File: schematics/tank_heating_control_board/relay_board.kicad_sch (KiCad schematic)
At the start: 30 parts, among them J1 Programming Header, J2 Power IN from battery, J3 Power OUT to heater, K1 AZ2150-1AE-24DEF, Q1 MMBF170, SW1 SW_DIP_x04, U1 JST I2C Connector, U2 JST I2C Connector, U3 PIC16F1826-ISO, U4 INA180A1

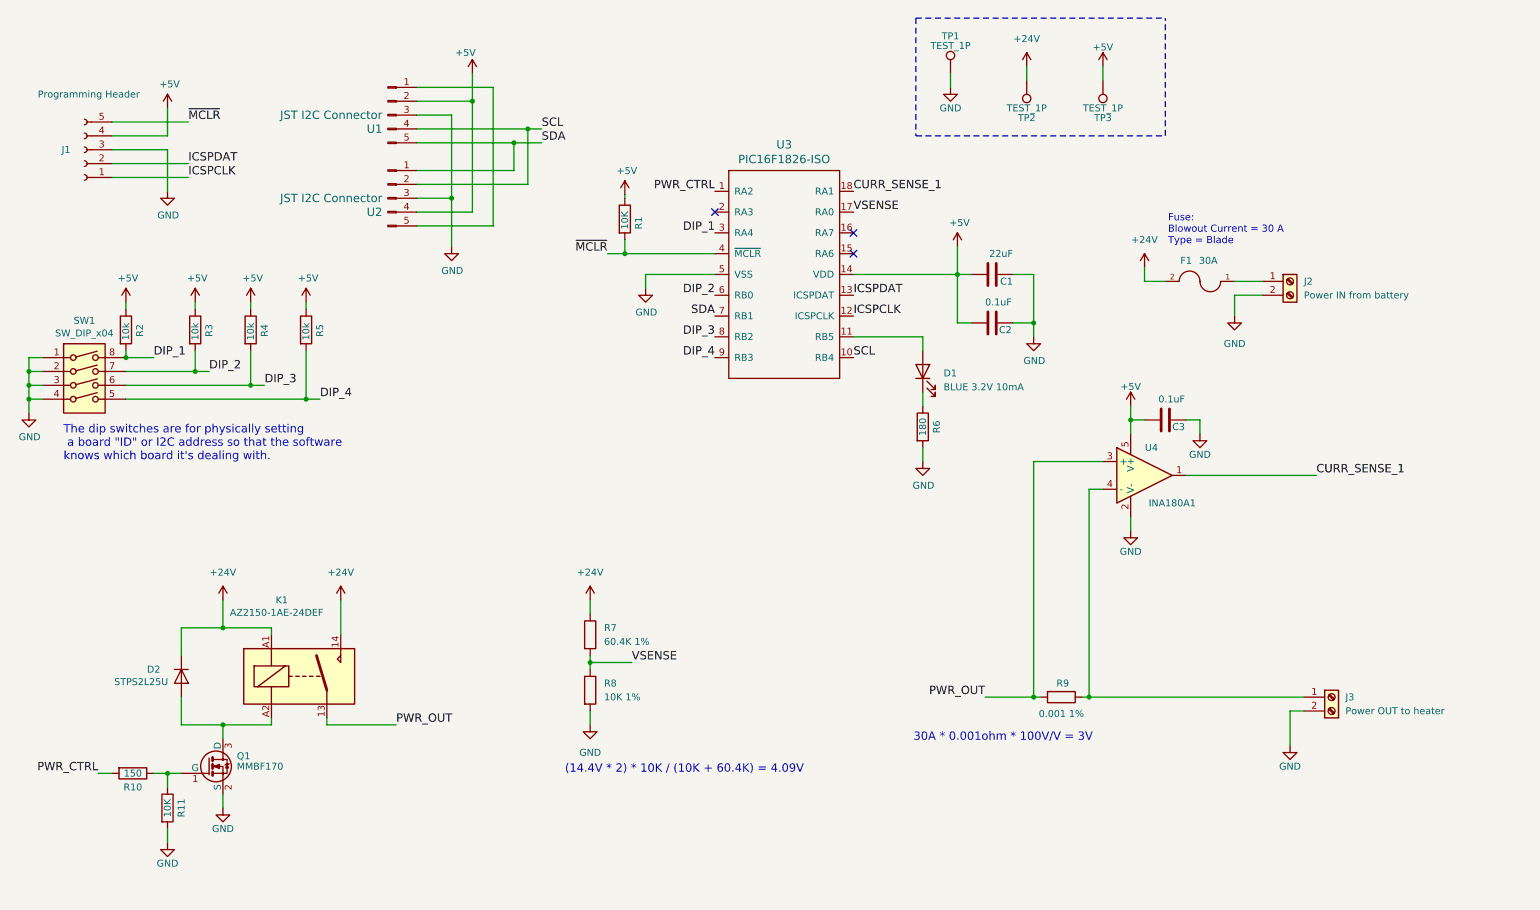
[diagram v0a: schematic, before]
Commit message: Add thermistor and voltage sensing to schematics
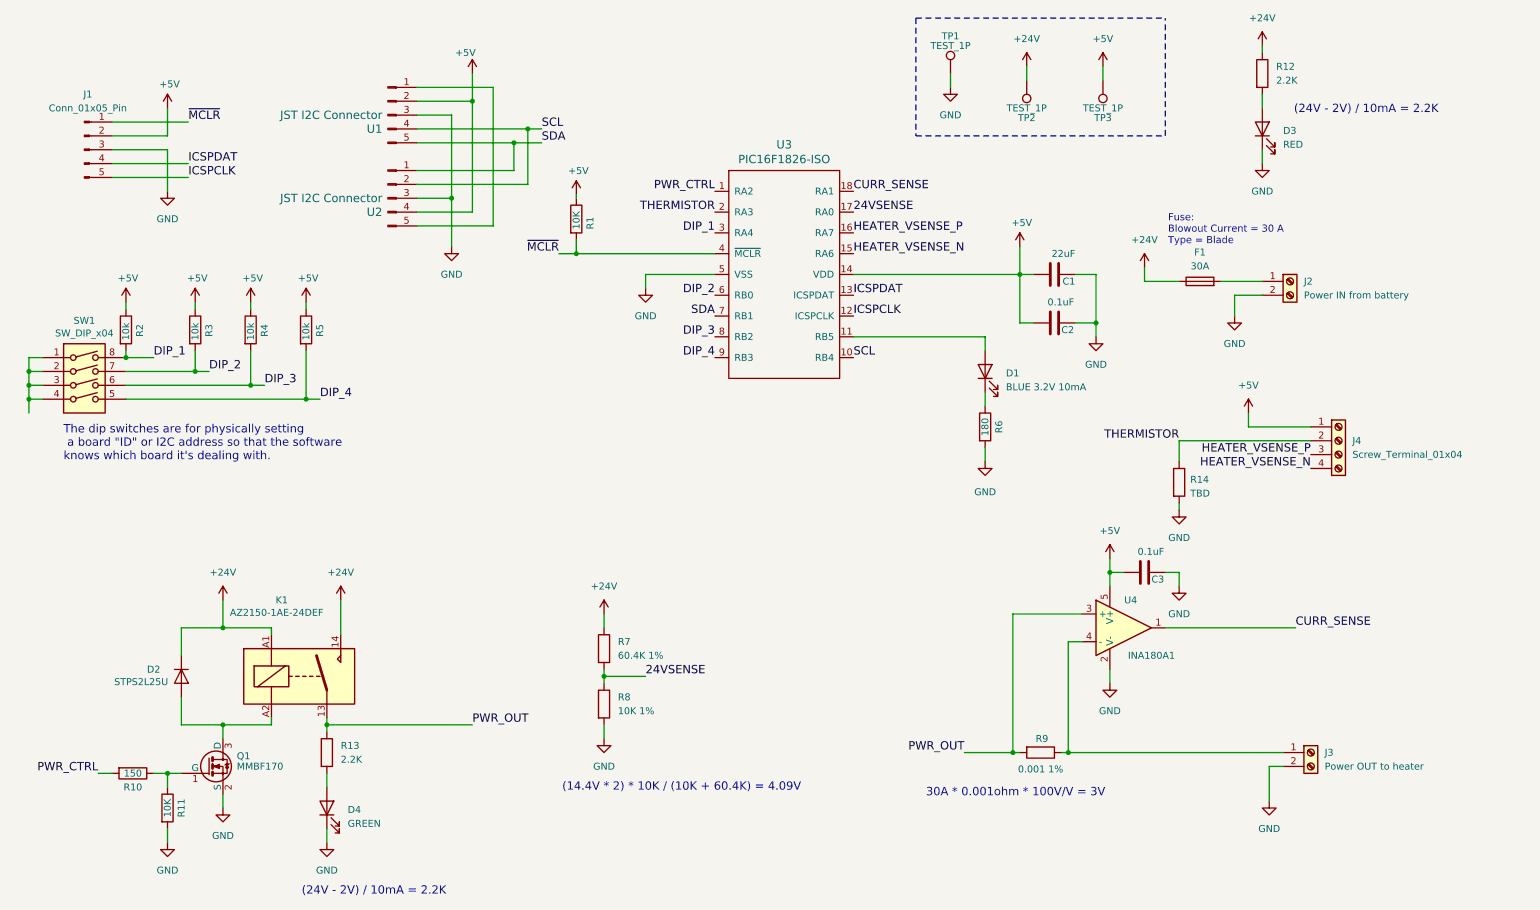
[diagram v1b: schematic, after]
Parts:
- removed F1: 30A, custom:littlefuse_01000020Z, symbol relay_board:FUSE-rlcs_relay_board
- removed J1: Programming Header, custom:PinHeader_5x2.54_SMD_90deg_952-3198-1-ND, symbol Connector:Conn_01x05_Female
- added D3: RED, LED_SMD:LED_1206_3216Metric_Pad1.42x1.75mm_HandSolder, symbol Device:LED
- added D4: GREEN, LED_SMD:LED_1206_3216Metric_Pad1.42x1.75mm_HandSolder, symbol Device:LED
- added F1: 30A, custom:3557-10_KEY, symbol Device:Fuse
- added J1: Conn_01x05_Pin, custom:PinHeader_5x2.54_SMD_90deg_952-3198-1-ND, symbol Connector:Conn_01x05_Pin
- added J4: Screw_Terminal_01x04, TerminalBlock_Phoenix:TerminalBlock_Phoenix_PT-1,5-4-5.0-H_1x04_P5.00mm_Horizontal, symbol Connector:Screw_Terminal_01x04
- added R12, R13: 2.2K, Resistor_SMD:R_0805_2012Metric_Pad1.20x1.40mm_HandSolder, symbol Device:R
- added R14: TBD, Resistor_SMD:R_0805_2012Metric_Pad1.20x1.40mm_HandSolder, symbol Device:R
- Q1: footprint Package_TO_SOT_SMD:SOT-23_Handsoldering -> Package_TO_SOT_SMD:SOT-23
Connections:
- net +24V: now also F1.1, R12.1
- net +5V: now also J1.2 (Pin_2), J4.1 (Pin_1)
- net GND: now also D3.1 (K), D4.1 (K), J1.3 (Pin_3), R14.2; no longer SW1.1, SW1.2, SW1.3, SW1.4
- net ICSPCLK: now also J1.5 (Pin_5)
- net ICSPDAT: now also J1.4 (Pin_4)
- net PWR_OUT: now also R13.1
- net ~{MCLR}: now also J1.1 (Pin_1)
- net HEATER_VSENSE_N: now reaches U3.15 (RA6)
- net HEATER_VSENSE_N: now also J4.4 (Pin_4)
- net HEATER_VSENSE_P: now reaches U3.16 (RA7)
- net HEATER_VSENSE_P: now also J4.3 (Pin_3)
- net THERMISTOR: now reaches U3.2 (RA3)
- net THERMISTOR: now also J4.2 (Pin_2), R14.1
- net at J2.1 (Pin_1): now also F1.2
- net CURR_SENSE_1 renamed CURR_SENSE
- net VSENSE renamed 24VSENSE
- new net: SW1.1, SW1.2, SW1.3, SW1.4
- new net: D4.2 (A), R13.2
- new net: D3.2 (A), R12.2
- no-connect marks 3 -> 0
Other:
- note added: "(24V - 2V) / 10mA = 2.2K"
- moved on the sheet: C1, C2, C3, D1, J3, R1, R6, R7, R8, R9, U4

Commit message: routed
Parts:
- removed J1: Conn_01x05_Pin, custom:PinHeader_5x2.54_SMD_90deg_952-3198-1-ND, symbol Connector:Conn_01x05_Pin
- added J1: Conn_01x05_Socket, custom:PinHeader_5x2.54_SMD_90deg_952-3198-1-ND, symbol Connector:Conn_01x05_Socket
- added R15, R17: 60.4K 1%, Resistor_SMD:R_0805_2012Metric_Pad1.20x1.40mm_HandSolder, symbol Device:R
- added R16, R18: 10K 1%, Resistor_SMD:R_0805_2012Metric_Pad1.20x1.40mm_HandSolder, symbol Device:R
- J4: value Screw_Terminal_01x04 -> Vsense and Thermistor
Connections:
- net +5V: now also J1.2 (Pin_2)
- net GND: now also SW1.1, SW1.2, SW1.3, SW1.4, J1.3 (Pin_3), R16.2, R18.2
- net HEATER_VSENSE_N: now also R17.2, R18.1; no longer J4.4 (Pin_4)
- net HEATER_VSENSE_P: now also R15.2, R16.1; no longer J4.3 (Pin_3)
- net ICSPCLK: now also J1.5 (Pin_5)
- net ICSPDAT: now also J1.4 (Pin_4)
- net ~{MCLR}: now also J1.1 (Pin_1)
- new net: J4.3 (Pin_3), R17.1
- new net: J4.4 (Pin_4), R15.1
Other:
- moved on the sheet: C3, J3, J4, R14, R9, U4

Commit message: Change current sense to low side
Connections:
- net GND: now also R9.1, U4.4 (-); no longer J3.2 (Pin_2)
- net PWR_OUT: now also J3.1 (Pin_1); no longer R9.2, U4.3 (+)
- net +12V: now reaches U1.1, U2.5
- new net: J3.2 (Pin_2), R9.2, U4.3 (+)
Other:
- moved on the sheet: C3, J3, R7, R8, R9, U4
